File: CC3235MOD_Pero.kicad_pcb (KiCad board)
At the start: 2 copper layers, 57.9 x 34.3 mm, 38 parts, among them J1 USB_B_Mini, J2 JTAG/SWD, SW1 Reset, SW2 SW_DIP_x03, SW3 User IO, U1 TLV1117-33, U2 CP2102N-A01-GQFN24, U3 CC3235MODSF12MOBR

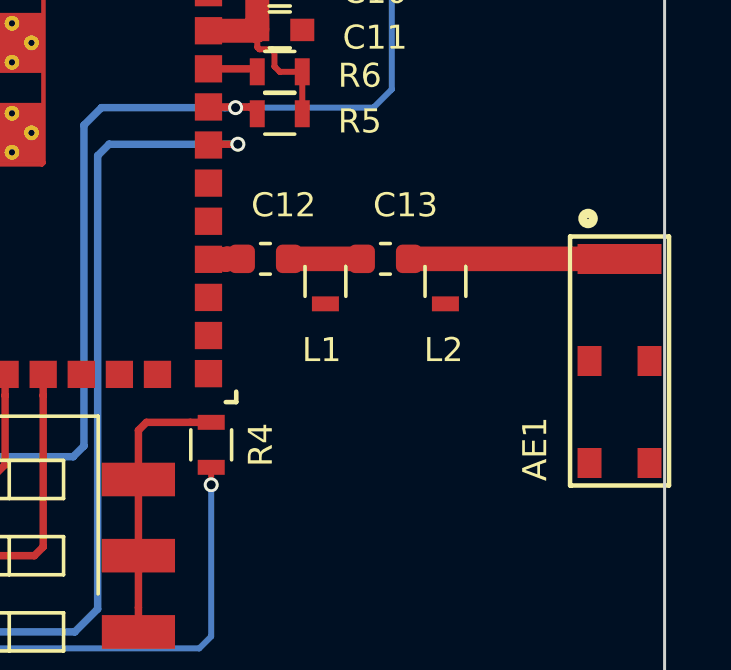
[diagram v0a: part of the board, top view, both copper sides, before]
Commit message: fixed rf filter placement
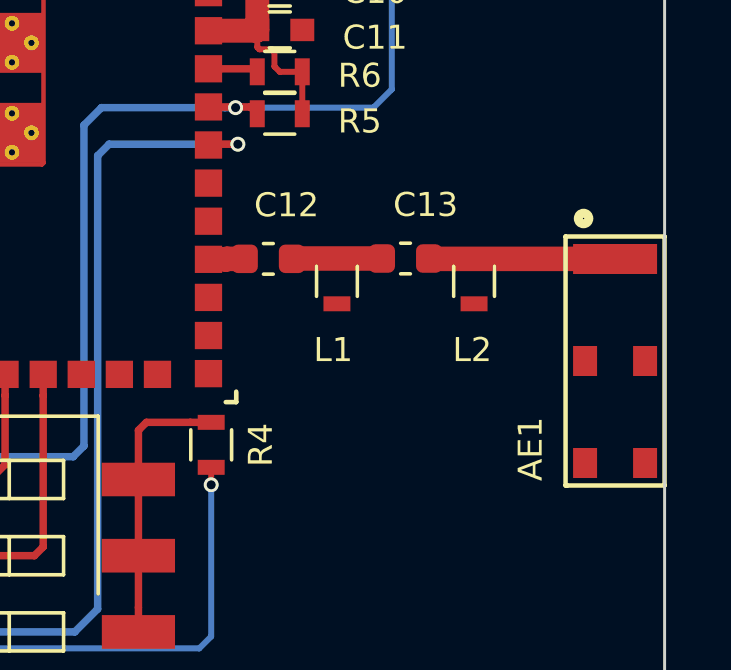
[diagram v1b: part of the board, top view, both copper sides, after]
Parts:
- moved L2 0.96 mm to (180.3, 108.5)
- moved C13 0.67 mm to (178.1, 107.7)
- moved L1 0.38 mm to (175.8, 108.5)
- moved AE1 0.15 mm to (185.0, 111.1)
- moved C12 0.10 mm to (173.5, 107.7)
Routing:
- net /ANTENNA: track 7.77 -> 7.11 mm
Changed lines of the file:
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@@
-(kicad_pcb (version 20171130) (host pcbnew "(5.0.0)")
+(kicad_pcb (version 20171130) (host pcbnew "(5.1.5)-3")
   (general
     (thickness 1.6)
     (drawings 6)
-    (tracks 279)
+    (tracks 280)
     (zones 0)
     (modules 38)
@@
   (layers
     (0 F.Cu signal)
-    (31 B.Cu signal hide)
+    (31 B.Cu signal)
     (32 B.Adhes user hide)
     (33 F.Adhes user)
@@
     (zone_45_only no)
     (trace_min 0.2)
-    (segment_width 0.2)
-    (edge_width 0.15)
     (via_size 0.5)
     (via_drill 0.3)
@@
     (uvia_min_size 0.2)
     (uvia_min_drill 0.1)
+    (edge_width 0.15)
+    (segment_width 0.2)
     (pcb_text_width 0.3)
     (pcb_text_size 0.8 1)
@@
   )
   (module Capacitor_SMD:C_0603_1608Metric (layer F.Cu)
-    (at 177.385 107.707 180)
+    (at 178.054 107.696 180)
     (descr "Capacitor SMD 0603 (1608 Metric), square (rectangular) end terminal, IPC_7351 nominal, (Body size source: http://www.tortai-tech.com/upload/download/2011102023233369053.pdf), generated with kicad-footprint-generator")
     (tags capacitor)
@@
   )
   (module Capacitor_SMD:C_0603_1608Metric (layer F.Cu)
-    (at 173.385 107.707 180)
+    (at 173.482 107.707 180)
     (descr "Capacitor SMD 0603 (1608 Metric), square (rectangular) end terminal, IPC_7351 nominal, (Body size source: http://www.tortai-tech.com/upload/download/2011102023233369053.pdf), generated with kicad-footprint-generator")
     (tags capacitor)
@@
   )
   (module footprints:M830520 (layer F.Cu)
-    (at 185.18886 111.1123 270)
+    (at 185.03886 111.1123 270)
     (fp_text reference AE1 (at 2.9337 2.81686 90) (layer F.SilkS)
       (effects (font (size 0.8 0.8) (thickness 0.15)))
@@
   )
   (module Inductors_SMD:L_0603 (layer F.Cu)
-    (at 175.385 108.457 270)
+    (at 175.768 108.457 270)
     (descr "Resistor SMD 0603, reflow soldering, Vishay (see dcrcw.pdf)")
     (tags "resistor 0603")
@@
   )
   (module Inductors_SMD:L_0603 (layer F.Cu)
-    (at 179.385 108.457 270)
+    (at 180.34 108.457 270)
     (descr "Resistor SMD 0603, reflow soldering, Vishay (see dcrcw.pdf)")
     (tags "resistor 0603")
@@
   (segment (start 150.533 99.822) (end 151.770999 99.822) (width 0.25) (layer F.Cu) (net 26) (status 30))
   (segment (start 150.533 102.87) (end 151.777 102.87) (width 0.25) (layer F.Cu) (net 27) (status 30))
-  (segment (start 184.18356 107.707) (end 184.18886 107.7123) (width 0.82) (layer F.Cu) (net 30) (status 30))
-  (segment (start 178.1725 107.707) (end 184.18356 107.707) (width 0.82) (layer F.Cu) (net 30) (status 30))
   (segment (start 185.58886 107.7123) (end 185.93999 107.7123) (width 1) (layer F.Cu) (net 30))
   (segment (start 184.18886 107.7123) (end 185.58886 107.7123) (width 1) (layer F.Cu) (net 30))
-  (segment (start 174.1725 107.707) (end 176.5975 107.707) (width 0.82) (layer F.Cu) (net 31) (status 30))
-  (zone (net 0) (net_name "") (layer F.Cu) (hatch edge 0.508)
-    (connect_pads yes (clearance 0.2))
-    (min_thickness 0.254)
-    (keepout (tracks allowed) (vias not_allowed) (copperpour not_allowed))
-    (fill (arc_segments 32) (thermal_gap 0.508) (thermal_bridge_width 0.508))
-    (polygon
-      (pts
-        (xy 186.59 115.96) (xy 182.1 116.03) (xy 182.1 108.8) (xy 182.6 108.8) (xy 182.6 106.45)
-        (xy 186.6 106.45)
-      )
-    )
-  )
+  (segment (start 178.8415 107.696) (end 178.8525 107.707) (width 0.82) (layer F.Cu) (net 30))
+  (segment (start 184.18356 107.707) (end 184.18886 107.7123) (width 0.82) (layer F.Cu) (net 30))
+  (segment (start 178.8525 107.707) (end 184.18356 107.707) (width 0.82) (layer F.Cu) (net 30))
+  (segment (start 174.359 107.696) (end 177.2665 107.696) (width 0.82) (layer F.Cu) (net 31))
   (zone (net 29) (net_name VBUS) (layer F.Cu) (hatch edge 0.508)
     (priority 2)
@@
     (polygon
       (pts
-        (xy 186.5906 115.96) (xy 182.1006 116.03) (xy 182.1006 108.8) (xy 182.6006 108.8) (xy 182.6006 106.45)
-        (xy 186.6006 106.45)
+        (xy 186.4406 115.96) (xy 181.9506 116.03) (xy 181.9506 108.8) (xy 182.4506 108.8) (xy 182.4506 106.45)
+        (xy 186.4506 106.45)
       )
     )

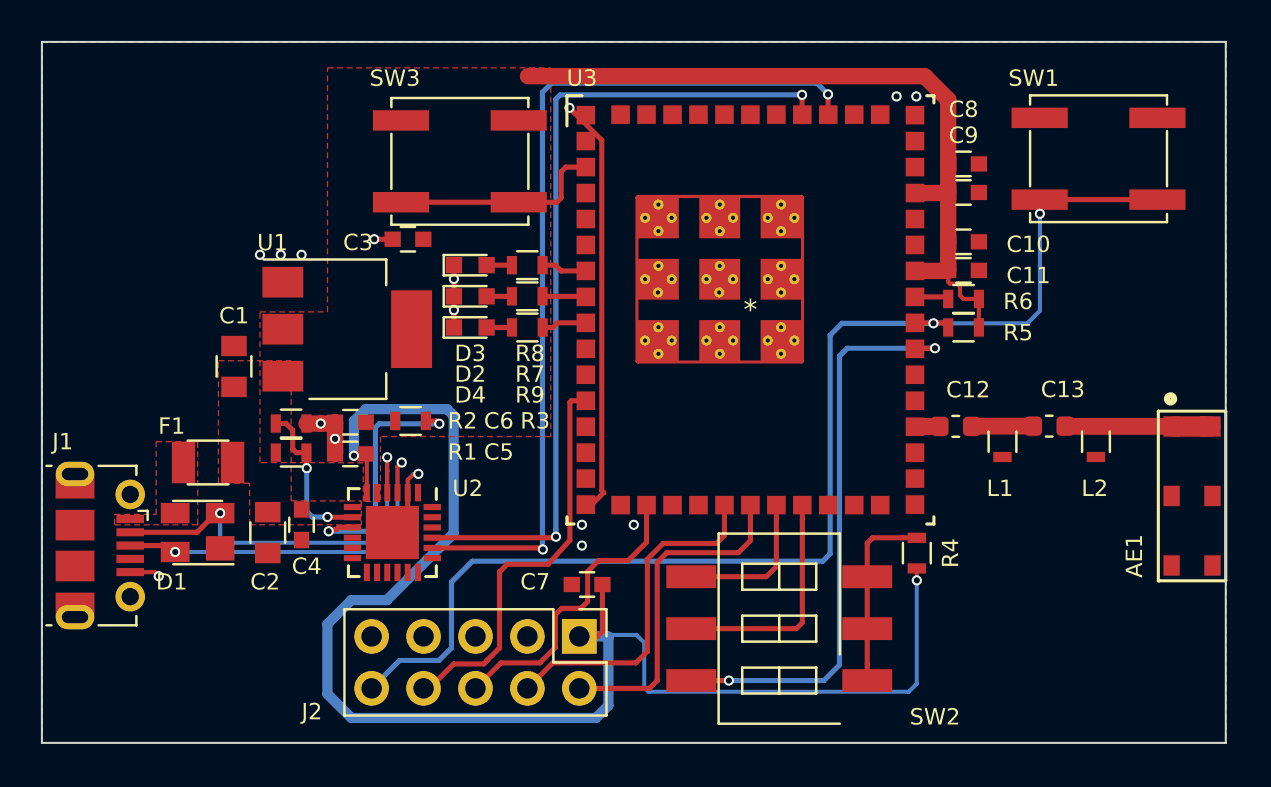
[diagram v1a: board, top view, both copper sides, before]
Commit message: antenna gnd solved
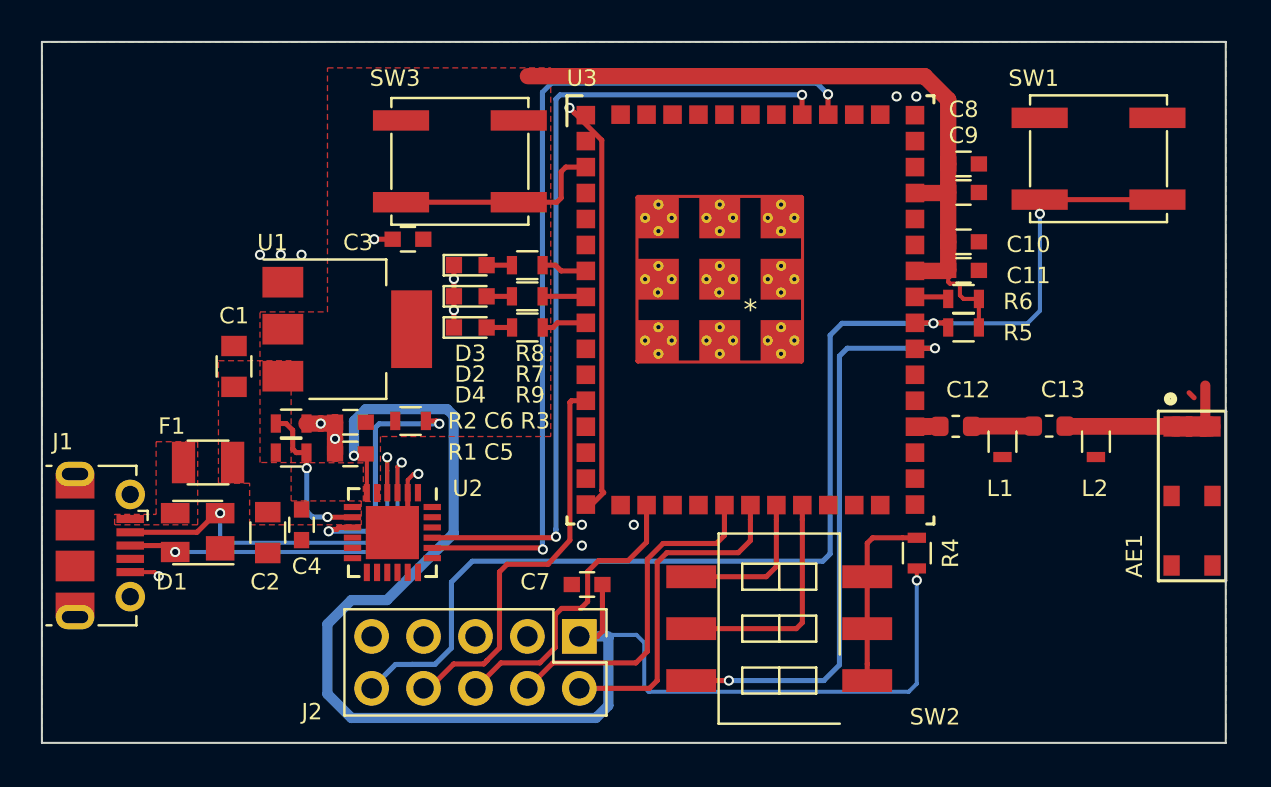
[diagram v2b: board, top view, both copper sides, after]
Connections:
- AE1 pad 1: /ANTENNA -> GND
- AE1 pad 2: /ANTENNA -> GND
- C13 pad 1: /ANTENNA -> GND
- L2 pad 1: /ANTENNA -> GND
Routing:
- net GND: track 31.6 -> 41.4 mm
- net /ANTENNA: track 7.11 -> 0.00 mm
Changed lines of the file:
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@@
     (thickness 1.6)
     (drawings 6)
-    (tracks 280)
+    (tracks 286)
     (zones 0)
     (modules 38)
-    (nets 32)
+    (nets 31)
   )
   (page A4)
@@
   )
   (setup
-    (last_trace_width 0.25)
+    (last_trace_width 0.5)
     (user_trace_width 0.2)
     (user_trace_width 0.25)
@@
   (net 28 "Net-(J1-Pad6)")
   (net 29 VBUS)
-  (net 30 /ANTENNA)
-  (net 31 /PI)
+  (net 30 /PI)
   (net_class Default "This is the default net class."
     (clearance 0.2)
@@
     (add_net "Net-(D3-Pad2)")
     (add_net "Net-(D4-Pad2)")
+    (add_net "Net-(J1-Pad4)")
     (add_net "Net-(J1-Pad6)")
     (add_net "Net-(J2-Pad10)")
@@
     (add_net "Net-(J2-Pad4)")
     (add_net "Net-(J2-Pad6)")
+    (add_net "Net-(J2-Pad7)")
     (add_net "Net-(J2-Pad8)")
     (add_net "Net-(R1-Pad1)")
@@
     (add_net "Net-(SW2-Pad6)")
     (add_net "Net-(SW3-Pad2)")
+    (add_net "Net-(U2-Pad1)")
+    (add_net "Net-(U2-Pad10)")
+    (add_net "Net-(U2-Pad11)")
+    (add_net "Net-(U2-Pad12)")
+    (add_net "Net-(U2-Pad13)")
+    (add_net "Net-(U2-Pad14)")
+    (add_net "Net-(U2-Pad15)")
+    (add_net "Net-(U2-Pad16)")
+    (add_net "Net-(U2-Pad17)")
+    (add_net "Net-(U2-Pad18)")
+    (add_net "Net-(U2-Pad19)")
+    (add_net "Net-(U2-Pad22)")
+    (add_net "Net-(U2-Pad23)")
+    (add_net "Net-(U2-Pad24)")
+    (add_net "Net-(U3-Pad10)")
+    (add_net "Net-(U3-Pad11)")
+    (add_net "Net-(U3-Pad13)")
+    (add_net "Net-(U3-Pad14)")
+    (add_net "Net-(U3-Pad15)")
+    (add_net "Net-(U3-Pad17)")
+    (add_net "Net-(U3-Pad19)")
+    (add_net "Net-(U3-Pad20)")
+    (add_net "Net-(U3-Pad33)")
+    (add_net "Net-(U3-Pad39)")
+    (add_net "Net-(U3-Pad4)")
+    (add_net "Net-(U3-Pad41)")
+    (add_net "Net-(U3-Pad42)")
+    (add_net "Net-(U3-Pad44)")
+    (add_net "Net-(U3-Pad45)")
+    (add_net "Net-(U3-Pad48)")
+    (add_net "Net-(U3-Pad49)")
+    (add_net "Net-(U3-Pad5)")
+    (add_net "Net-(U3-Pad50)")
+    (add_net "Net-(U3-Pad51)")
+    (add_net "Net-(U3-Pad52)")
+    (add_net "Net-(U3-Pad53)")
+    (add_net "Net-(U3-Pad54)")
+    (add_net "Net-(U3-Pad6)")
     (add_net VBUS)
   )
@@
     (uvia_dia 0.3)
     (uvia_drill 0.1)
-    (add_net /ANTENNA)
     (add_net /PI)
     (add_net /RF_OUT)
@@
     (fp_line (start -0.8 0.4) (end -0.8 -0.4) (layer F.Fab) (width 0.1))
     (pad 2 smd roundrect (at 0.7875 0 180) (size 0.875 0.95) (layers F.Cu F.Paste F.Mask) (roundrect_rratio 0.25)
-      (net 31 /PI))
+      (net 30 /PI))
     (pad 1 smd roundrect (at -0.7875 0 180) (size 0.875 0.95) (layers F.Cu F.Paste F.Mask) (roundrect_rratio 0.25)
-      (net 30 /ANTENNA))
+      (net 1 GND))
     (model ${KISYS3DMOD}/Capacitor_SMD.3dshapes/C_0603_1608Metric.wrl
       (at (xyz 0 0 0))
@@
       (net 8 /RF_OUT))
     (pad 1 smd roundrect (at -0.7875 0 180) (size 0.875 0.95) (layers F.Cu F.Paste F.Mask) (roundrect_rratio 0.25)
-      (net 31 /PI))
+      (net 30 /PI))
     (model ${KISYS3DMOD}/Capacitor_SMD.3dshapes/C_0603_1608Metric.wrl
       (at (xyz 0 0 0))
@@
     (fp_circle (center -4.75 1.05) (end -4.65 1.05) (layer F.SilkS) (width 0.15))
     (pad 1 smd rect (at -3.4 1 270) (size 1 0.8) (layers F.Cu F.Paste F.Mask)
-      (net 30 /ANTENNA))
+      (net 1 GND))
     (pad 2 smd rect (at -3.4 -1 270) (size 1 0.8) (layers F.Cu F.Paste F.Mask)
-      (net 30 /ANTENNA))
+      (net 1 GND))
     (pad 3 smd rect (at 0 -1 270) (size 1 0.8) (layers F.Cu F.Paste F.Mask))
     (pad 4 smd rect (at 3.4 -1 270) (size 1 0.8) (layers F.Cu F.Paste F.Mask))
@@
     (fp_line (start -0.5 -0.68) (end 0.5 -0.68) (layer F.SilkS) (width 0.12))
     (pad 1 smd rect (at -0.75 0 270) (size 0.5 0.9) (layers F.Cu F.Paste F.Mask)
-      (net 31 /PI))
+      (net 30 /PI))
     (pad 2 smd rect (at 0.75 0 270) (size 0.5 0.9) (layers F.Cu F.Paste F.Mask)
       (net 1 GND))
@@
       (net 1 GND))
     (pad 1 smd rect (at -0.75 0 270) (size 0.5 0.9) (layers F.Cu F.Paste F.Mask)
-      (net 30 /ANTENNA))
+      (net 1 GND))
     (model ${KISYS3DMOD}/Inductors_SMD.3dshapes/L_0603.wrl
       (at (xyz 0 0 0))
@@
   (segment (start 177.5968 96.6248) (end 177.587 96.615) (width 0.2) (layer F.Cu) (net 10) (status 30))
   (segment (start 177.5968 97.3074) (end 177.5968 96.6248) (width 0.2) (layer F.Cu) (net 10) (status 20))
+  (segment (start 146.882999 119.347999) (end 148.011001 119.347999) (width 0.25) (layer B.Cu) (net 10))
+  (segment (start 167.3352 113.9444) (end 167.3352 103.251) (width 0.25) (layer B.Cu) (net 10))
+  (segment (start 146.876398 119.3546) (end 146.882999 119.347999) (width 0.25) (layer B.Cu) (net 10))
+  (segment (start 146.0754 119.3546) (end 146.876398 119.3546) (width 0.25) (layer B.Cu) (net 10))
   (segment (start 172.036247 102.6668) (end 172.3898 102.6668) (width 0.25) (layer B.Cu) (net 10))
-  (segment (start 167.9194 102.6668) (end 172.036247 102.6668) (width 0.25) (layer B.Cu) (net 10))
   (segment (start 167.3352 103.251) (end 167.9194 102.6668) (width 0.25) (layer B.Cu) (net 10))
+  (segment (start 167.9194 102.6668) (end 172.036247 102.6668) (width 0.25) (layer B.Cu) (net 10))
+  (segment (start 144.907 120.523) (end 146.0754 119.3546) (width 0.25) (layer B.Cu) (net 10))
   (segment (start 166.976589 114.303011) (end 167.3352 113.9444) (width 0.25) (layer B.Cu) (net 10))
-  (segment (start 167.3352 113.9444) (end 167.3352 103.251) (width 0.25) (layer B.Cu) (net 10))
-  (segment (start 149.831589 114.303011) (end 166.976589 114.303011) (width 0.25) (layer B.Cu) (net 10))
-  (segment (start 144.907 120.523) (end 146.271999 119.158001) (width 0.25) (layer B.Cu) (net 10) (status 10))
-  (segment (start 148.200999 119.158001) (end 148.811999 118.547001) (width 0.25) (layer B.Cu) (net 10))
+  (segment (start 148.011001 119.347999) (end 148.811999 118.547001) (width 0.25) (layer B.Cu) (net 10))
   (segment (start 148.811999 118.547001) (end 148.811999 115.322601) (width 0.25) (layer B.Cu) (net 10))
-  (segment (start 146.271999 119.158001) (end 148.200999 119.158001) (width 0.25) (layer B.Cu) (net 10))
   (segment (start 148.811999 115.322601) (end 149.831589 114.303011) (width 0.25) (layer B.Cu) (net 10))
+  (segment (start 149.831589 114.303011) (end 166.976589 114.303011) (width 0.25) (layer B.Cu) (net 10))
   (segment (start 173.013202 101.373202) (end 173.113 101.473) (width 0.25) (layer F.Cu) (net 11) (status 30))
   (segment (start 171.486202 101.373202) (end 173.013202 101.373202) (width 0.25) (layer F.Cu) (net 11) (status 30))
@@
   (segment (start 150.533 99.822) (end 151.770999 99.822) (width 0.25) (layer F.Cu) (net 26) (status 30))
   (segment (start 150.533 102.87) (end 151.777 102.87) (width 0.25) (layer F.Cu) (net 27) (status 30))
-  (segment (start 185.58886 107.7123) (end 185.93999 107.7123) (width 1) (layer F.Cu) (net 30))
-  (segment (start 184.18886 107.7123) (end 185.58886 107.7123) (width 1) (layer F.Cu) (net 30))
-  (segment (start 178.8415 107.696) (end 178.8525 107.707) (width 0.82) (layer F.Cu) (net 30))
-  (segment (start 184.18356 107.707) (end 184.18886 107.7123) (width 0.82) (layer F.Cu) (net 30))
-  (segment (start 178.8525 107.707) (end 184.18356 107.707) (width 0.82) (layer F.Cu) (net 30))
-  (segment (start 174.359 107.696) (end 177.2665 107.696) (width 0.82) (layer F.Cu) (net 31))
+  (segment (start 185.58886 107.7123) (end 185.93999 107.7123) (width 1) (layer F.Cu) (net 1))
+  (segment (start 178.8415 107.696) (end 178.8525 107.707) (width 0.82) (layer F.Cu) (net 1))
+  (segment (start 184.18356 107.707) (end 184.18886 107.7123) (width 0.82) (layer F.Cu) (net 1))
+  (segment (start 178.8525 107.707) (end 184.18356 107.707) (width 0.82) (layer F.Cu) (net 1))
+  (segment (start 184.8957 107.7123) (end 185.58886 107.7123) (width 1) (layer F.Cu) (net 1))
+  (segment (start 184.18886 107.7123) (end 184.8957 107.7123) (width 1) (layer F.Cu) (net 1))
+  (segment (start 185.1406 106.3062) (end 184.8957 106.0613) (width 0.25) (layer F.Cu) (net 1))
+  (segment (start 184.8957 107.7123) (end 185.1406 107.4674) (width 0.25) (layer F.Cu) (net 1))
+  (segment (start 185.68886 107.7123) (end 185.68886 105.71114) (width 0.5) (layer F.Cu) (net 1))
+  (segment (start 174.359 107.696) (end 177.2665 107.696) (width 0.82) (layer F.Cu) (net 30))
   (zone (net 29) (net_name VBUS) (layer F.Cu) (hatch edge 0.508)
     (priority 2)
